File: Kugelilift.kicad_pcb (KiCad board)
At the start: 2 copper layers, 43 x 43.5 mm, 16 parts, among them J2 TTL, J4 Stepper, SW1 RESET, SW2 MODE, SW3 SW_Push, SW4 SW_DIP_x04, SW5 SW_Push, U1 magnetic-charger, U2 TCRT5000, U3 ULN2003A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

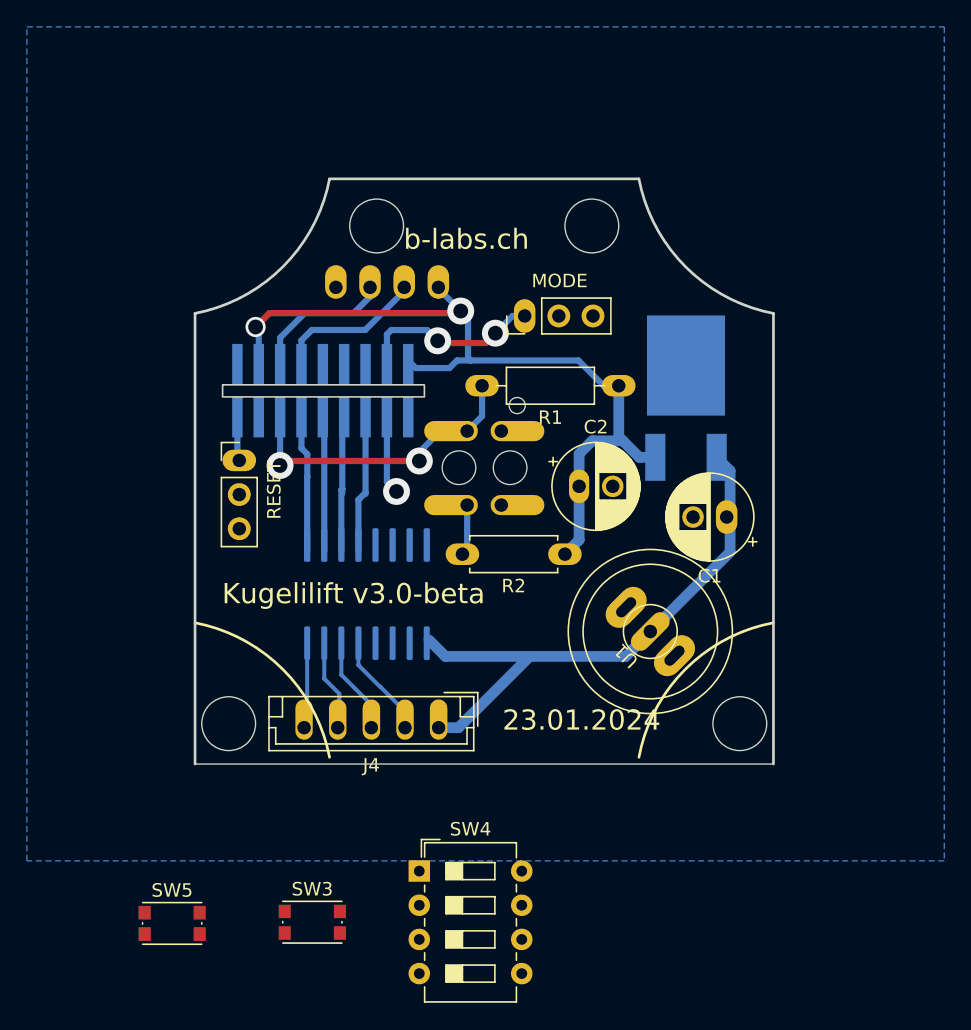
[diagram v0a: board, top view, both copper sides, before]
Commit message: Laid out pushbuttons and dip switches
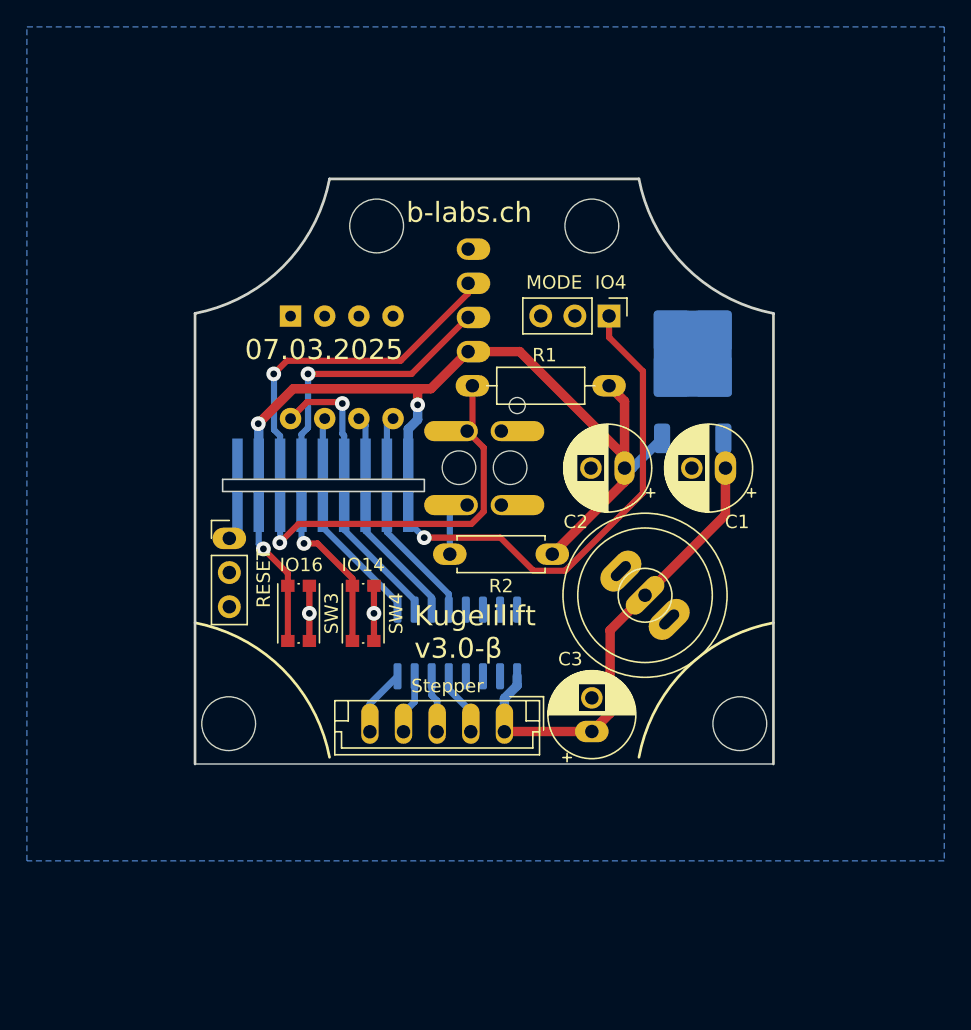
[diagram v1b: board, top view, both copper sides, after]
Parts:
- added C3: C_Polarized, Capacitor_THT:CP_Radial_D6.3mm_P2.50mm, F.Cu at (130.0, 97.6)
- SW5: renamed from SW4; moved to B.Cu
- U3: footprint Package_SO:SOP-16_4.55x10.3mm_P1.27mm -> Package_SO:SOIC-16_3.9x9.9mm_P1.27mm
- moved SW5 42.4 mm to (107.6, 66.7), turned to -90 degrees
- moved SW4 27.1 mm to (113.0, 88.8), turned to -90 degrees
- moved SW3 23.0 mm to (108.2, 88.8), turned to -90 degrees
- moved J2 10.2 mm to (120.8, 61.7), turned to 180 degrees
- moved U3 7.64 mm to (120.0, 91.0)
- moved U6 7.03 mm to (110.0, 79.3)
- moved SW2 6.27 mm to (131.3, 66.7), turned to -90 degrees
- moved SW1 5.84 mm to (103.0, 83.2)
- moved J4 4.90 mm to (123.5, 97.6)
- moved C2 3.64 mm to (132.4, 78.0), turned to 180 degrees
- moved C1 3.64 mm to (139.9, 78.0)
- moved U1 2.72 mm to (134.0, 87.5)
- moved U5 2.30 mm to (137.5, 70.8)
- moved R2 0.94 mm to (127.1, 84.4)
- moved R1 0.72 mm to (131.3, 71.9)
- renumbered SW5 to SW4
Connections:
- net Net-(J4-Pad2) renamed /MOTOR4
- net Net-(J4-Pad3) renamed /MOTOR3
- net Net-(J4-Pad4) renamed /MOTOR2
- net Net-(J4-Pad5) renamed /MOTOR1
- SW2 pad 1: Net-(SW2-Pad1) -> SW2
- SW3 pad 1: unconnected-(SW3-Pad1) -> GND
- SW3 pad 2: unconnected-(SW3-Pad2) -> SW3
- SW4 pad 1: unconnected-(SW5-Pad1) -> GND
- SW4 pad 2: unconnected-(SW5-Pad2) -> SW5
- SW5 pad 1: unconnected-(SW4-Pad1) -> GND
- SW5 pad 2: unconnected-(SW4-Pad2) -> GND
- SW5 pad 3: unconnected-(SW4-Pad3) -> GND
- SW5 pad 4: unconnected-(SW4-Pad4) -> GND
- SW5 pad 5: unconnected-(SW4-Pad5) -> DIP4
- SW5 pad 6: unconnected-(SW4-Pad6) -> DIP3
- SW5 pad 7: unconnected-(SW4-Pad7) -> DIP2
- SW5 pad 8: unconnected-(SW4-Pad8) -> DIP1
- U3 pad 5: unconnected-(U3-Pad5) -> GND
- U3 pad 6: unconnected-(U3-Pad6) -> GND
- U3 pad 7: unconnected-(U3-Pad7) -> GND
- U6 pad 10: unconnected-(U6-Pad10) -> SW2
- U6 pad 11: unconnected-(U6-Pad11) -> /in-4
- U6 pad 12: /in-4 -> /in-3
- U6 pad 13: /in-3 -> /in-2
- U6 pad 14: /in-2 -> /in-1
- U6 pad 15: /in-1 -> SW5
- U6 pad 17: unconnected-(U6-Pad17) -> SW3
- U6 pad 5: unconnected-(U6-Pad5) -> DIP2
- U6 pad 6: unconnected-(U6-Pad6) -> DIP1
- U6 pad 7: unconnected-(U6-Pad7) -> DIP3
- U6 pad 8: Net-(SW2-Pad1) -> DIP4
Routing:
- net SW2: track 0.00 -> 36.3 mm, vias 0 -> 1
- net TX: track 10.6 -> 24.2 mm, vias 0 -> 1
- net Net-(SW2-Pad1): track 13.5 -> 0.00 mm, vias 2 -> 0
- net SW5: track 0.00 -> 11.8 mm, vias 0 -> 1
- net SW3: track 0.00 -> 10.5 mm, vias 0 -> 1
- net RX: track 10.9 -> 20.1 mm, vias 0 -> 1
- net DIP1: track 0.00 -> 8.56 mm, vias 0 -> 1
- net GND: track 0.00 -> 8.20 mm, vias 0 -> 2
- net Net-(U6-ADC): track 22.0 -> 28.5 mm, vias 2 -> 1
- net unconnected-(U6-Pad11): track 5.81 -> 0.00 mm, vias 1 -> 0
- net +5V: track 42.5 -> 37.0 mm
- net /MOTOR4: track 8.13 -> 4.80 mm
- net /MOTOR3: track 7.60 -> 4.29 mm
- net DIP3: track 0.00 -> 3.19 mm
- net DIP4: track 0.00 -> 3.17 mm
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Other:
- board text added: "07.03.2025"
- board text added: "Kugelilift v3.0-β"
- board text removed: "23.01.2024"
- board text removed: "Kugelilift v3.0-beta"

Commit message: Update to "hard" pushbuttons, rearrange components.
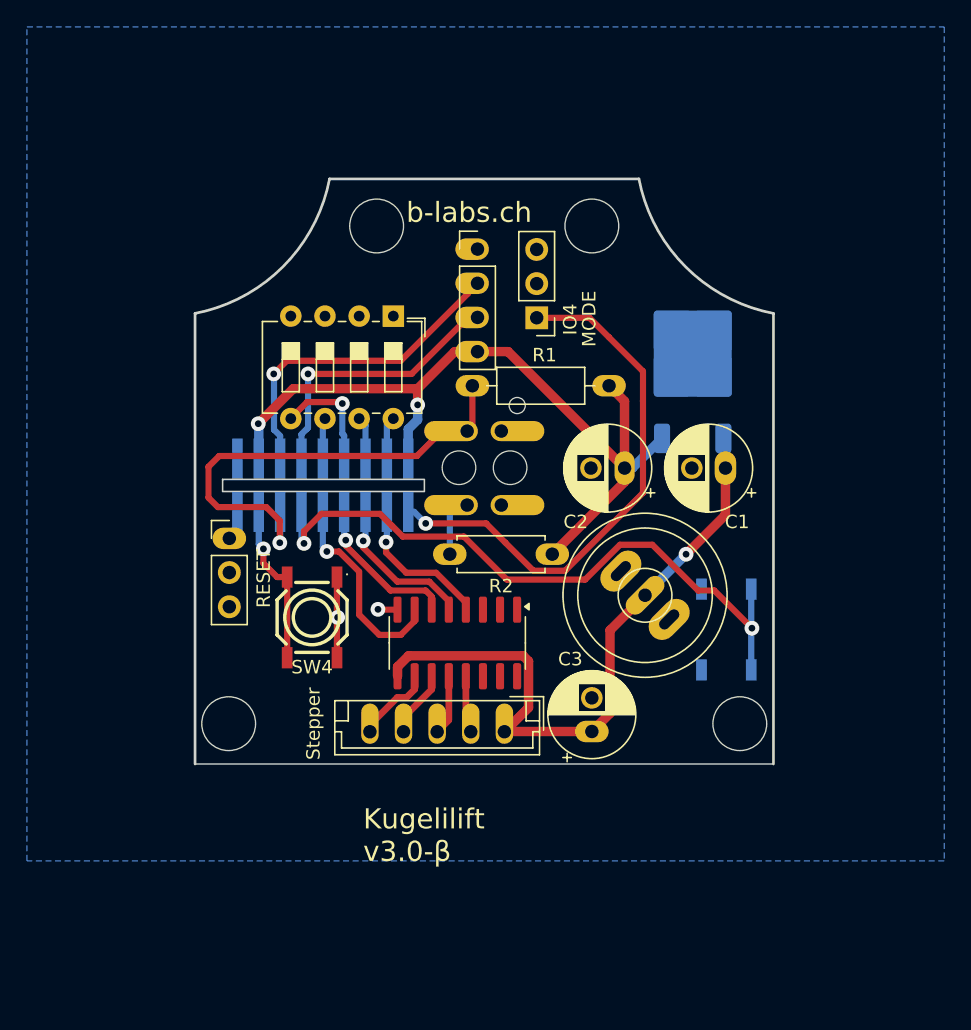
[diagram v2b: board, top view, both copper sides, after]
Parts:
- J2, SW5, U3: moved to F.Cu
- SW3: value SW_Push -> GT-TZ084B-H015-L1; footprint Button_Switch_SMD:SW_Push_1P1T_NO_CK_KMR2 -> jlc_footprints:SW-SMD_4P-L5.2-W5.2-P3.70-LS6.4; moved to B.Cu
- SW4: value SW_Push -> GT-TZ084B-H015-L1; footprint Button_Switch_SMD:SW_Push_1P1T_NO_CK_KMR2 -> jlc_footprints:SW-SMD_4P-L5.2-W5.2-P3.70-LS6.4
- moved SW3 31.8 mm to (140.0, 90.0)
- moved SW5 7.64 mm to (115.2, 66.7)
- moved SW2 5.38 mm to (125.9, 66.8), turned to 180 degrees
- moved SW4 3.81 mm to (109.2, 89.1)
- moved J2 0.70 mm to (121.5, 61.7), turned to 0 degrees
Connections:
- SW2 pad 3: (no net) -> unconnected-(SW2-Pin_3-Pad3)
- SW3 pad 2: SW3 -> GND
- SW4 pad 2: SW5 -> GND
- SW5 pad 5: DIP4 -> DIP1
- SW5 pad 6: DIP3 -> DIP2
- SW5 pad 7: DIP2 -> DIP3
- SW5 pad 8: DIP1 -> DIP4
- U3 pad 1: /in-1 -> unconnected-(U3-I1-Pad1)
- U3 pad 10: unconnected-(U3-O7-Pad10) -> /MOTOR1
- U3 pad 11: unconnected-(U3-O6-Pad11) -> /MOTOR2
- U3 pad 12: unconnected-(U3-O5-Pad12) -> /MOTOR3
- U3 pad 14: /MOTOR3 -> unconnected-(U3-O3-Pad14)
- U3 pad 15: /MOTOR2 -> unconnected-(U3-O2-Pad15)
- U3 pad 16: /MOTOR1 -> unconnected-(U3-O1-Pad16)
- U3 pad 2: /in-2 -> unconnected-(U3-I2-Pad2)
- U3 pad 3: /in-3 -> unconnected-(U3-I3-Pad3)
- U3 pad 5: GND -> /in-3
- U3 pad 6: GND -> /in-2
- U3 pad 7: GND -> /in-1
- U6 pad 15: SW5 -> SW3
- U6 pad 17: SW3 -> SW4
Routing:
- net SW3: track 10.5 -> 48.8 mm, vias 1 -> 2
- net +5V: track 37.0 -> 49.4 mm, vias 0 -> 1
- net SW4: track 0.00 -> 12.2 mm, vias 0 -> 1
- net SW5: track 11.8 -> 0.00 mm, vias 1 -> 0
- net Net-(U6-ADC): track 28.5 -> 36.1 mm
- net /in-1: track 9.58 -> 16.5 mm, vias 0 -> 1
- net SW2: track 36.3 -> 40.3 mm
- net /in-3: track 9.31 -> 11.4 mm, vias 0 -> 1
- net /in-2: track 9.44 -> 11.5 mm, vias 0 -> 1
- net /in-4: track 9.18 -> 11.1 mm, vias 0 -> 1
- net /MOTOR1: track 4.98 -> 5.90 mm
- net GND: track 8.20 -> 7.47 mm
- net /MOTOR4: track 4.80 -> 4.28 mm
- net /MOTOR2: track 4.47 -> 4.99 mm
- net +3V3: track 60.6 -> 60.1 mm

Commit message: Rearrange components.
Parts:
- added SW32: GT-TZ084B-H015-L1, jlc_footprints:SW-SMD_4P-L5.2-W5.2-P3.70-LS6.4, F.Cu at (135.0, 97.0)
- SW3: moved to F.Cu
- U5: value UA78M33_TO252 -> AMS1117CD-3.3
- moved SW2 15.8 mm to (132.3, 81.3)
- moved U1 12.0 mm to (122.0, 87.6), turned to 0 degrees
- moved C2 11.5 mm to (134.7, 89.3)
- moved R2 10.3 mm to (128.3, 74.2), turned to -90 degrees
- moved U3 9.86 mm to (110.2, 90.3)
- moved C1 5.40 mm to (141.0, 83.3)
- moved SW4 5.30 mm to (109.2, 83.8), turned to 0 degrees
- moved U5 4.28 mm to (138.7, 74.9)
- moved J4 3.80 mm to (119.7, 97.6)
- moved J2 3.75 mm to (120.4, 65.3), turned to 90 degrees
- moved C3 2.80 mm to (127.2, 97.6)
- moved R1 1.83 mm to (129.6, 71.2)
- moved SW3 1.49 mm to (141.0, 91.1)
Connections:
- SW4 pad 4: SW4 -> unconnected-(SW4-Pad4)
- U3 pad 1: unconnected-(U3-I1-Pad1) -> /in-4
- U3 pad 10: /MOTOR1 -> unconnected-(U3-O7-Pad10)
- U3 pad 11: /MOTOR2 -> unconnected-(U3-O6-Pad11)
- U3 pad 12: /MOTOR3 -> unconnected-(U3-O5-Pad12)
- U3 pad 13: /MOTOR4 -> /MOTOR1
- U3 pad 14: unconnected-(U3-O3-Pad14) -> /MOTOR2
- U3 pad 15: unconnected-(U3-O2-Pad15) -> /MOTOR3
- U3 pad 16: unconnected-(U3-O1-Pad16) -> /MOTOR4
- U3 pad 2: unconnected-(U3-I2-Pad2) -> /in-3
- U3 pad 3: unconnected-(U3-I3-Pad3) -> /in-2
- U3 pad 4: /in-4 -> /in-1
- U3 pad 5: /in-3 -> unconnected-(U3-I5-Pad5)
- U3 pad 6: /in-2 -> unconnected-(U3-I6-Pad6)
- U3 pad 7: /in-1 -> unconnected-(U3-I7-Pad7)
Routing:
- net +3V3: track 60.1 -> 4.76 mm, vias 2 -> 0
- net +5V: track 49.4 -> 0.00 mm, vias 1 -> 0
- net SW3: track 48.8 -> 0.00 mm, vias 2 -> 0
- net SW2: track 40.3 -> 0.00 mm, vias 1 -> 0
- net Net-(U6-ADC): track 36.1 -> 0.00 mm, vias 1 -> 0
- net TX: track 24.2 -> 1.69 mm, vias 1 -> 0
- net RX: track 20.1 -> 1.81 mm, vias 1 -> 0
- net /in-1: track 16.5 -> 0.00 mm, vias 1 -> 0
- net SW4: track 12.2 -> 0.00 mm, vias 1 -> 0
- net /in-2: track 11.5 -> 0.00 mm, vias 1 -> 0
- net /in-3: track 11.4 -> 0.00 mm, vias 1 -> 0
- net /in-4: track 11.1 -> 0.00 mm, vias 1 -> 0
- net GND: track 7.47 -> 0.00 mm, vias 2 -> 0
- net DIP1: track 8.56 -> 1.71 mm, vias 1 -> 0
- net /MOTOR1: track 5.90 -> 0.00 mm
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
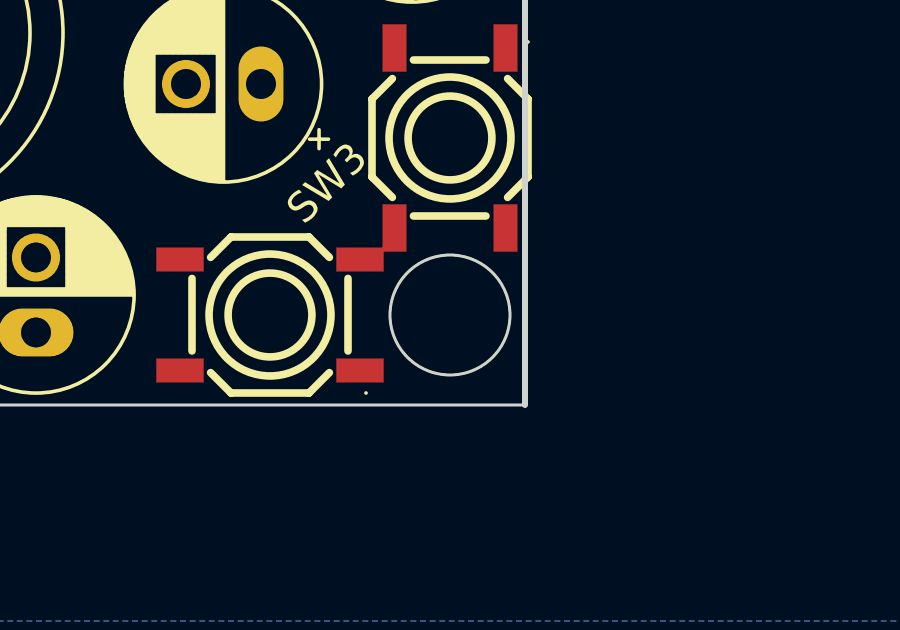
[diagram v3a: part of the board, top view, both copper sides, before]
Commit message: Use the LED footprint.
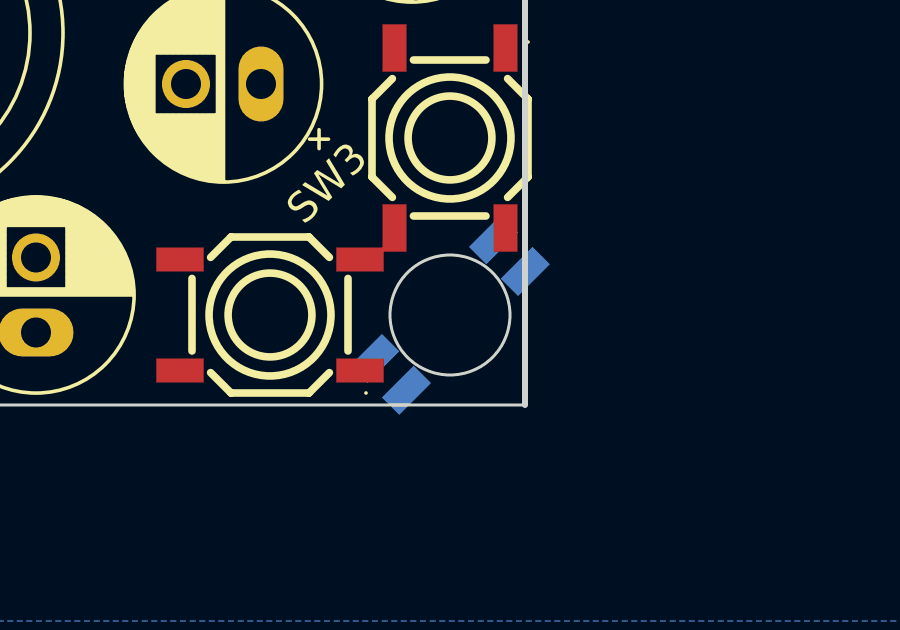
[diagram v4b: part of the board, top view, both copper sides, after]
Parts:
- added U4: SK6812MINI-E_C5149201, jlc_footprints:LED-SMD_L3.2-W2.8-LS5.9_SK6812MINI-E BACK, B.Cu at (141.0, 97.0)
